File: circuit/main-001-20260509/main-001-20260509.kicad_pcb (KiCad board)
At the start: 2 copper layers, 43.3 x 83.2 mm, 20 parts, among them J1 Conn_Relay, J2 Conn_Sub, Q1 BSS138, Q2 BSS138, SW1 RESET, U1 DEV-16771, U2 BNO055

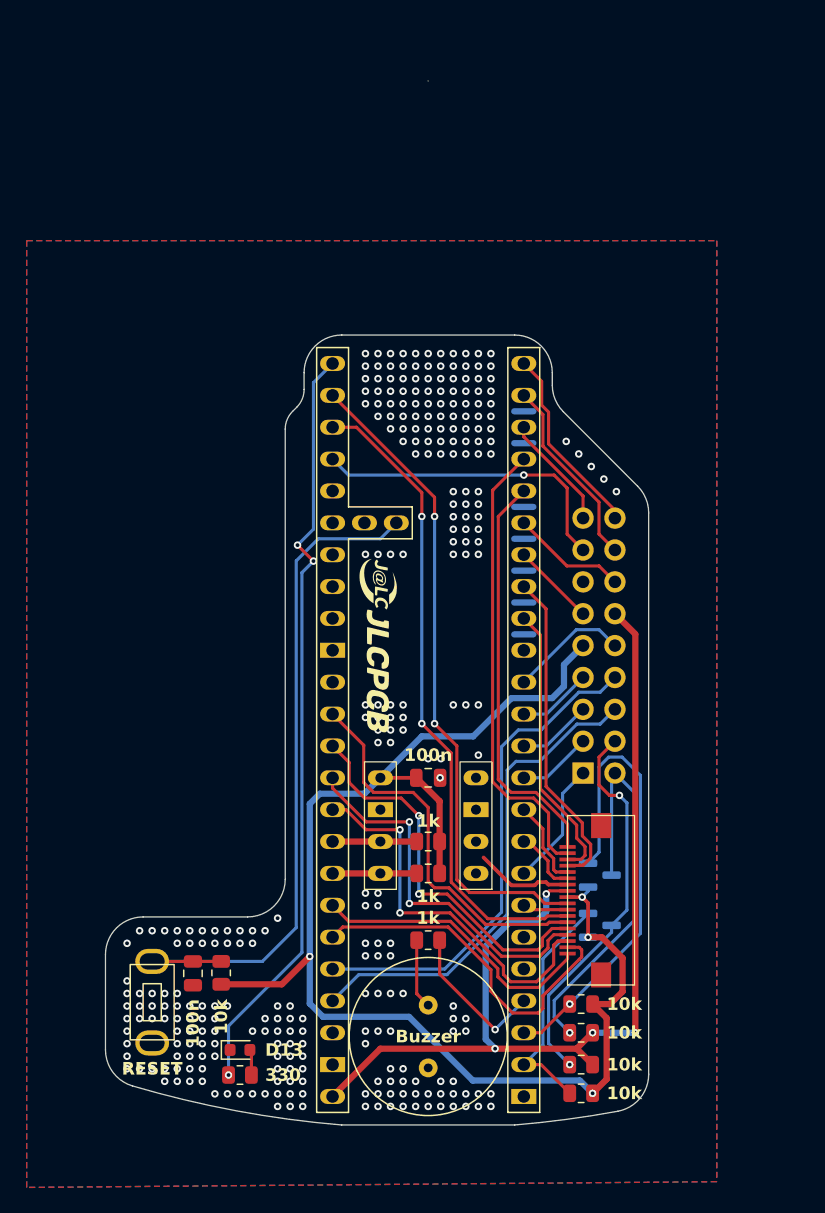
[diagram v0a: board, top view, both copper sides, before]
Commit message: Update メイン基板のシルクスクリーンを修正した
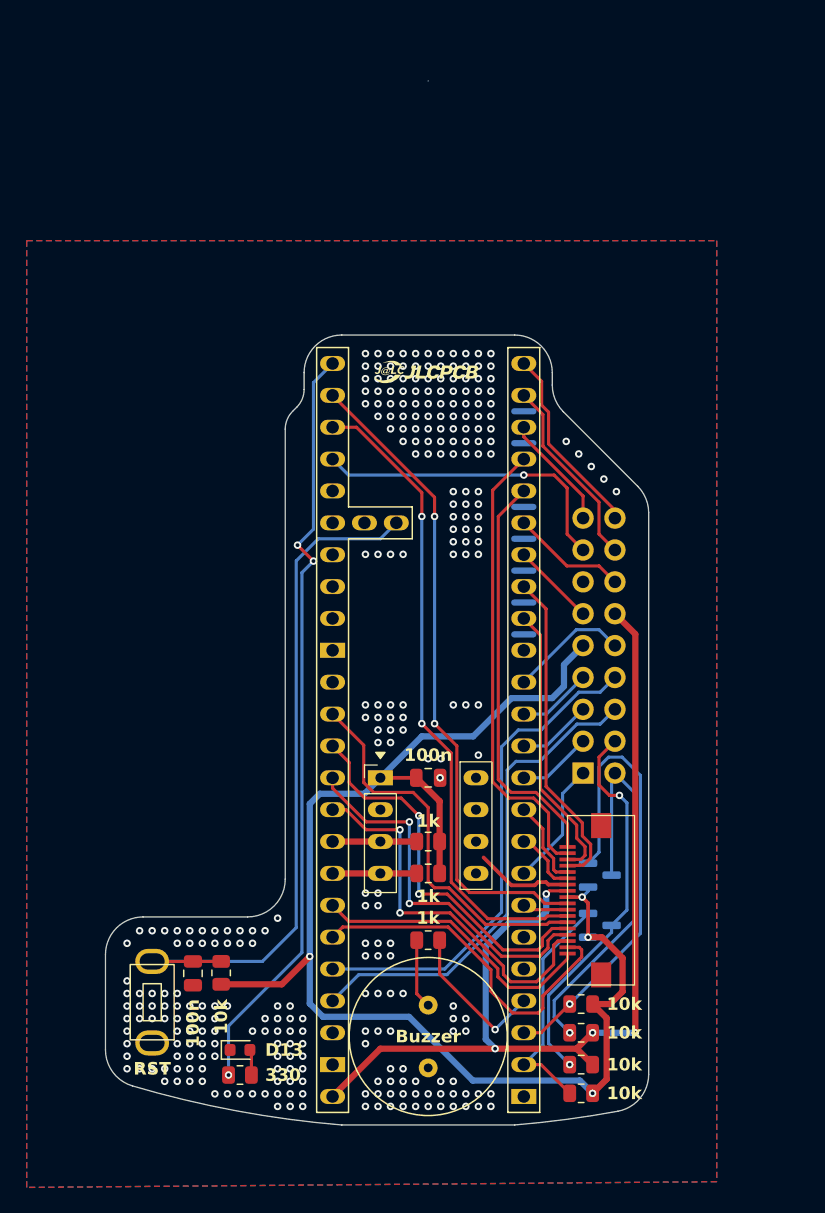
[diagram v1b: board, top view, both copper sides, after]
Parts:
- SW1: value RESET -> RST
- U2: value BNO055 -> Val**

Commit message: Update メイン基板の発注ファイルを更新
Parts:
- U2: value Val** -> BNO055
- moved J2 0.18 mm to (108.6, 119.1)
- moved C1 0.18 mm to (95.1, 109.3)
- moved J1 0.18 mm to (107.5, 109.0)
- moved Q1 0.18 mm to (108.8, 121.1)
- moved Q2 0.18 mm to (108.8, 117.1)
- moved R1 0.18 mm to (107.3, 134.5)
- moved R3 0.18 mm to (107.3, 132.2)
- moved R4 0.18 mm to (107.3, 129.7)
- moved U2 0.18 mm to (95.1, 113.2)
- moved C2 0.18 mm to (76.4, 124.9)
- moved R2 0.18 mm to (107.3, 127.4)
- moved R5 0.18 mm to (95.1, 114.4)
- moved R6 0.18 mm to (95.1, 122.3)
- moved R7 0.18 mm to (95.1, 117.0)
- moved R8 0.18 mm to (78.6, 124.9)
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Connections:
- net EN_{BOOST} renamed EN_{Boost}
- J2 pad 11: +5V -> GND
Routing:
- net +5V: track 79.8 -> 62.1 mm, vias 4 -> 3
- net GND: track 18.5 -> 28.8 mm

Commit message: Update メイン基板の回路図/ボード図/発注ファイルを更新
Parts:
- SW1: value RST -> RESET
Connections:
- J2 pad 10: +3.3V -> GND
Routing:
- net GND: track 28.8 -> 30.5 mm
- net +3.3V: track 111.2 -> 109.6 mm

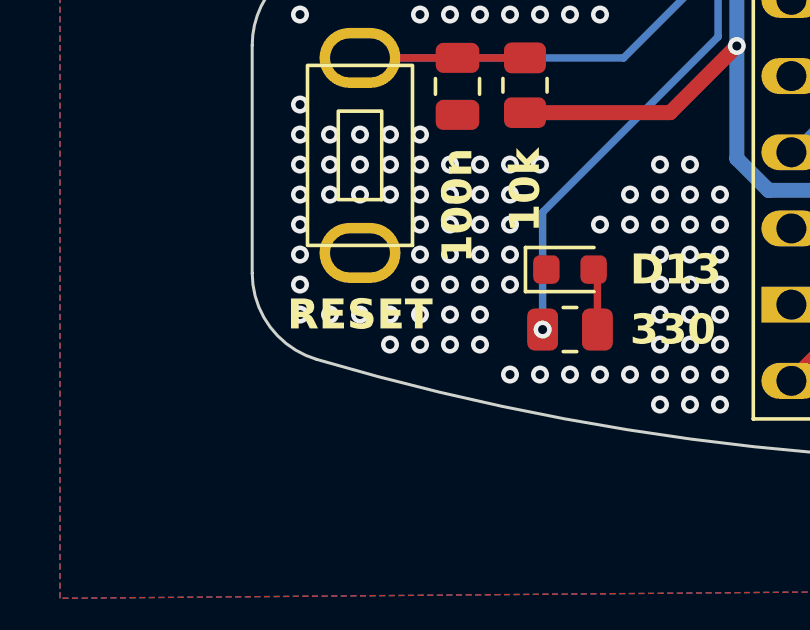
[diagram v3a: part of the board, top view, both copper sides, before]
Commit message: Update メイン基板の各種PDF、3Dファイル、発注ファイルを更新
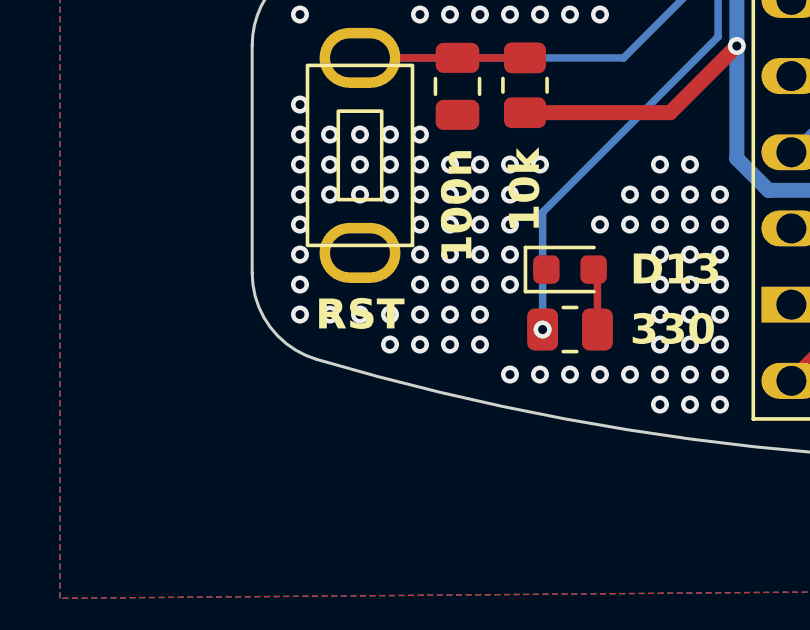
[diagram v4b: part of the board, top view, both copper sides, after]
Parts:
- SW1: value RESET -> RST

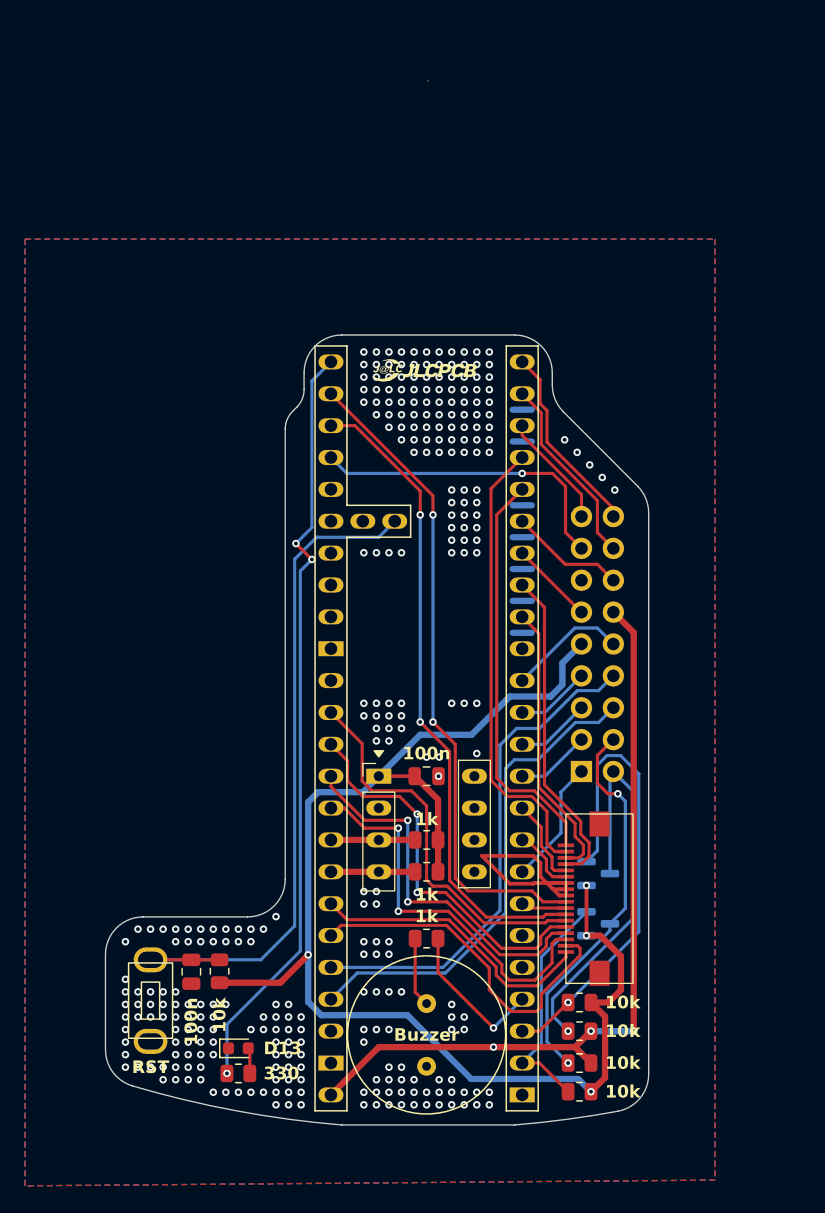
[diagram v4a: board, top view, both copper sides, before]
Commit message: Update メイン基板のボード図を修正
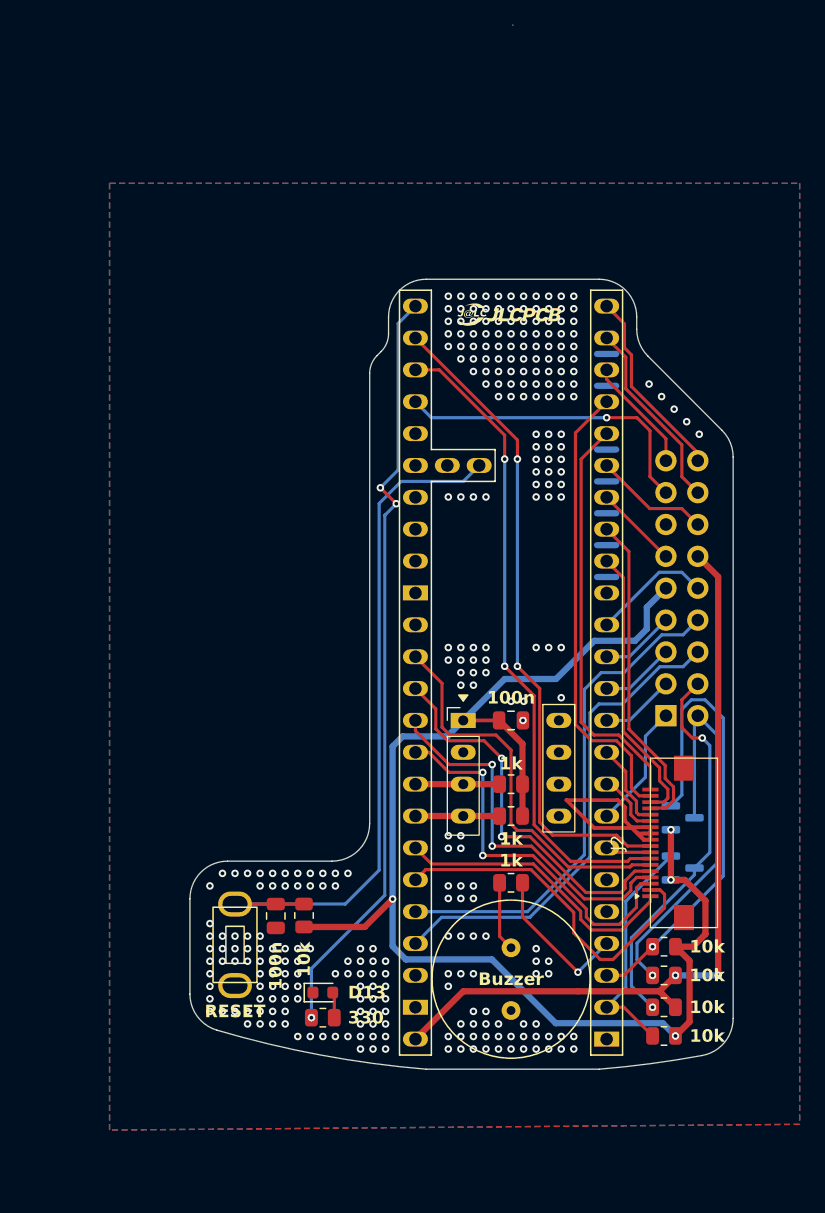
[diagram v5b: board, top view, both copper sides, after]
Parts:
- SW1: value RST -> RESET
- moved J2 8.07 mm to (115.3, 114.7)
- moved Q1 8.07 mm to (115.5, 116.7)
- moved Q2 8.07 mm to (115.5, 112.7)
- moved R1 8.07 mm to (114.0, 130.0)
- moved R2 8.07 mm to (114.0, 122.9)
- moved R3 8.07 mm to (114.0, 127.8)
- moved BZ1 8.07 mm to (101.9, 125.5)
- moved C2 8.07 mm to (83.1, 120.5)
- moved D1 8.07 mm to (86.9, 126.6)
- moved R4 8.07 mm to (114.0, 125.2)
- moved R5 8.07 mm to (101.9, 110.0)
- moved R6 8.07 mm to (101.9, 117.8)
- moved R8 8.07 mm to (85.4, 120.4)
- moved U1 8.07 mm to (101.9, 101.1)
- moved C1 8.07 mm to (101.9, 104.9)
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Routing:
- net GND: track 30.5 -> 30.3 mm, vias 292 -> 291
- net +5V: vias 3 -> 2

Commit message: Update メイン基板の発注ファイルを更新
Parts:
- SW1: value RESET -> RST
